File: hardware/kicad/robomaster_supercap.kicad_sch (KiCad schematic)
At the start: 0 parts

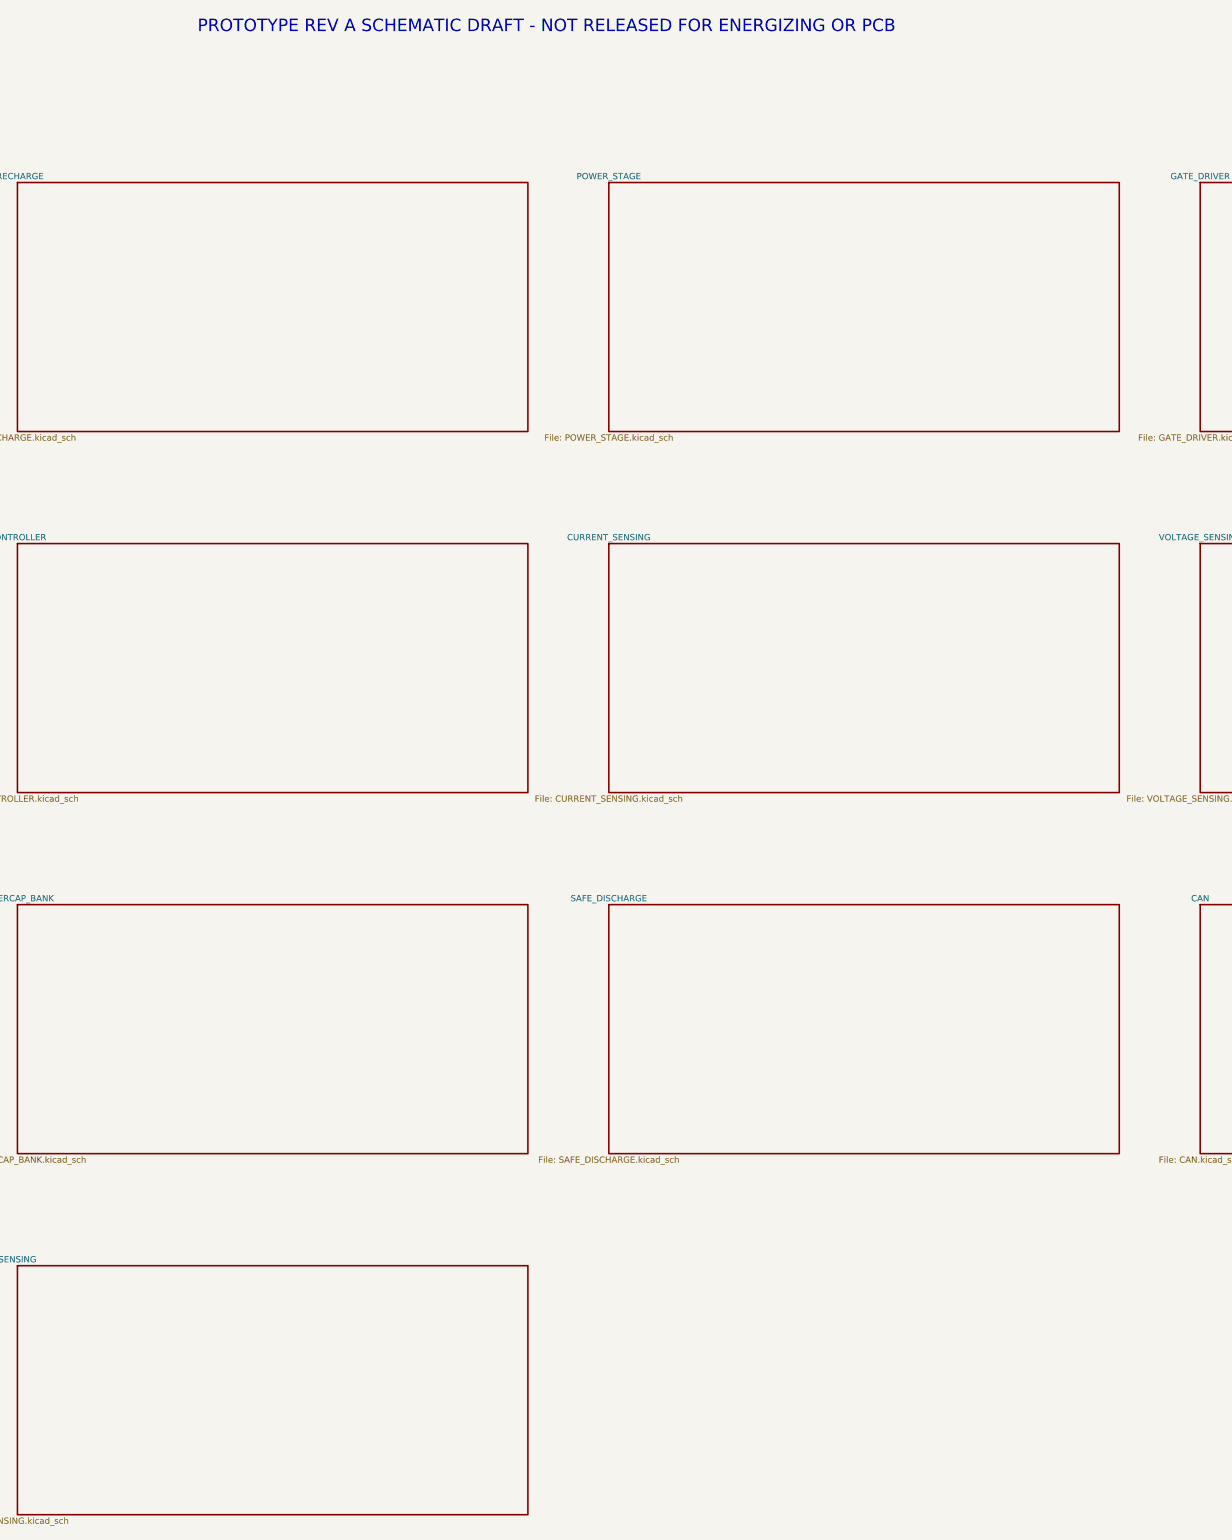
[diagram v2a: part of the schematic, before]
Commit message: hardware: define PCB harness boundary and Kelvin nets
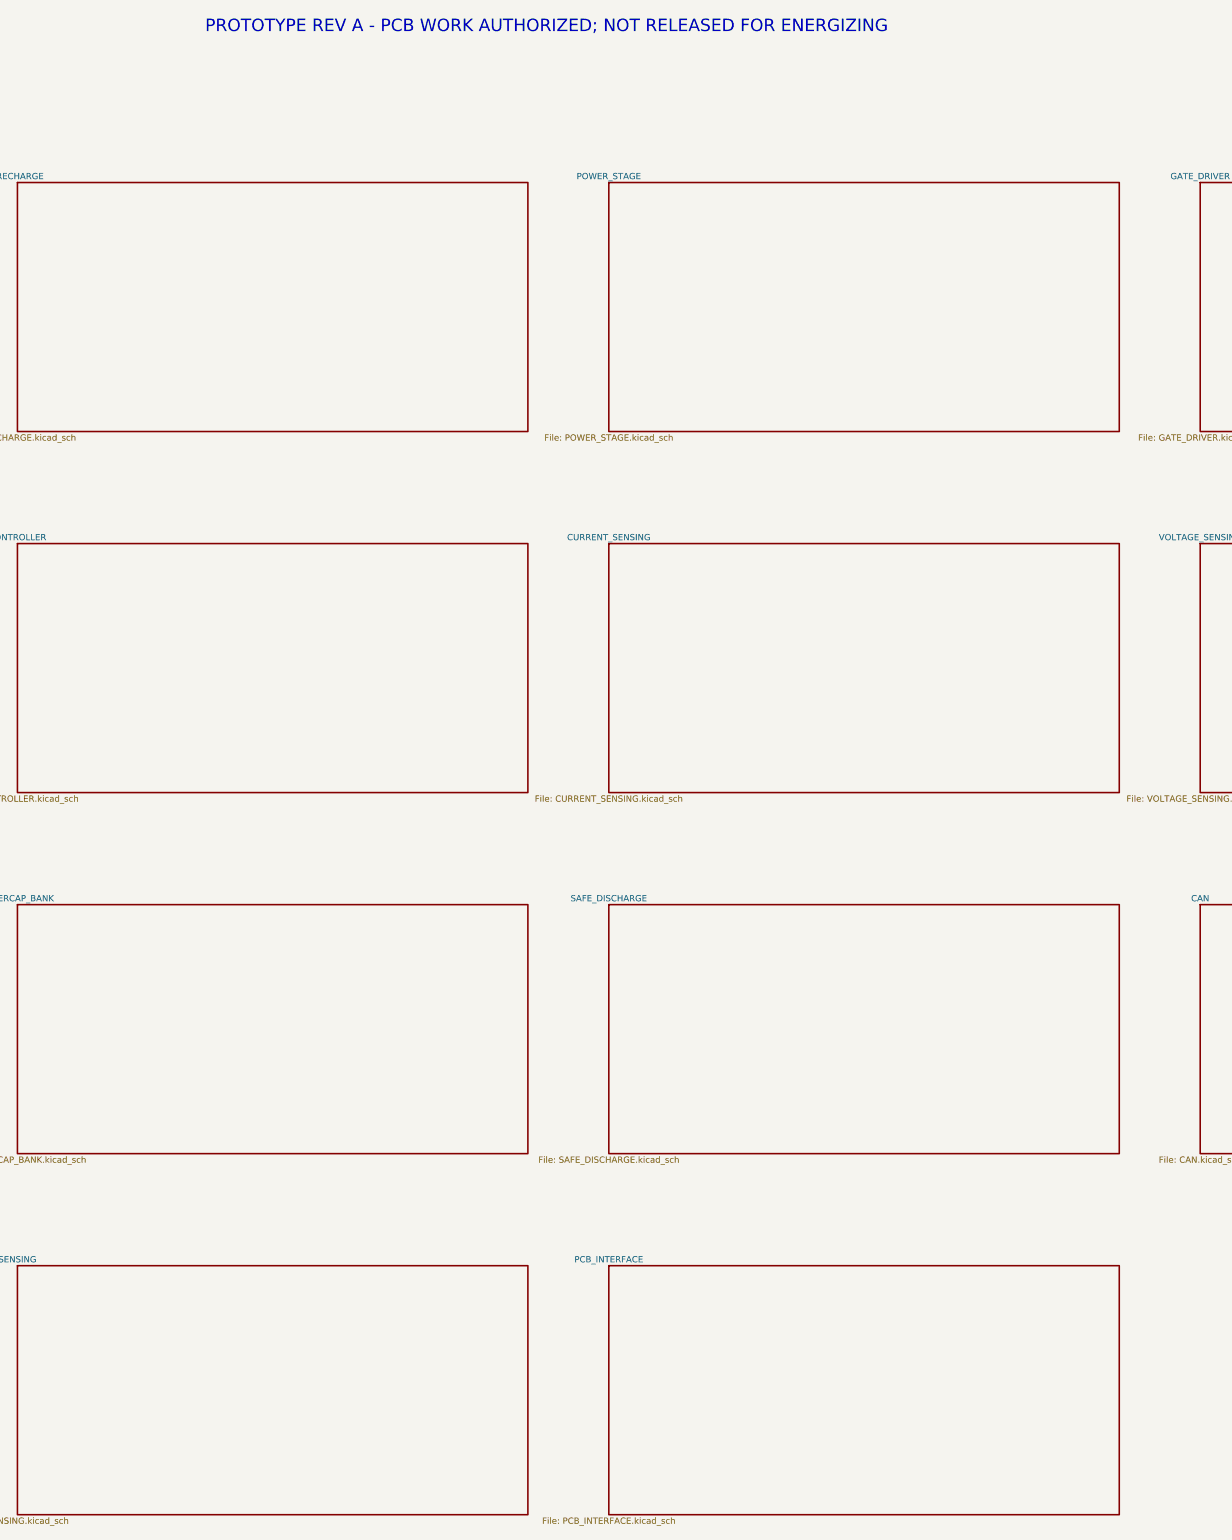
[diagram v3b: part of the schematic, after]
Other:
- added sheet PCB_INTERFACE (PCB_INTERFACE.kicad_sch)
- note added: "PROTOTYPE REV A - PCB WORK AUTHORIZED; NOT RELEASED FOR ENERGIZING"
- note removed: "PROTOTYPE REV A SCHEMATIC DRAFT - NOT RELEASED FOR ENERGIZING OR PCB"
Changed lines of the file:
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@@
   (generator "eeschema")
   (paper "A3")
-  (text "PROTOTYPE REV A SCHEMATIC DRAFT - NOT RELEASED FOR ENERGIZING OR PCB" (at 200 15 0) (effects (font (size 2 2))))
+  (text "PROTOTYPE REV A - PCB WORK AUTHORIZED; NOT RELEASED FOR ENERGIZING" (at 200 15 0) (effects (font (size 2 2))))
   (sheet
     (at 20 40)
@@
     (instances (project "robomaster_supercap" (path "/fe0d835f-f536-483b-a54a-4b6f1f4699ec" (page "15"))))
   )
+  (sheet
+    (at 210 214)
+    (size 82 40)
+    (stroke (width 0.254) (type default))
+    (fill (color 0 0 0 0))
+    (property "Sheetname" "PCB_INTERFACE" (at 210 213 0) (effects (font (size 1 1))))
+    (property "Sheetfile" "PCB_INTERFACE.kicad_sch" (at 210 255 0) (effects (font (size 1 1))))
+    (instances (project "robomaster_supercap" (path "/fe0d835f-f536-483b-a54a-4b6f1f4699ec" (page "16"))))
+  )
   (sheet_instances (path "/" (page "1")))
